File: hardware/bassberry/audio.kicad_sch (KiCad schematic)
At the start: 47 parts, among them J201 SAT LEFT, J202 SAT RIGHT, J203 SUB, U201 TAS5805M, U202 TAS5805M

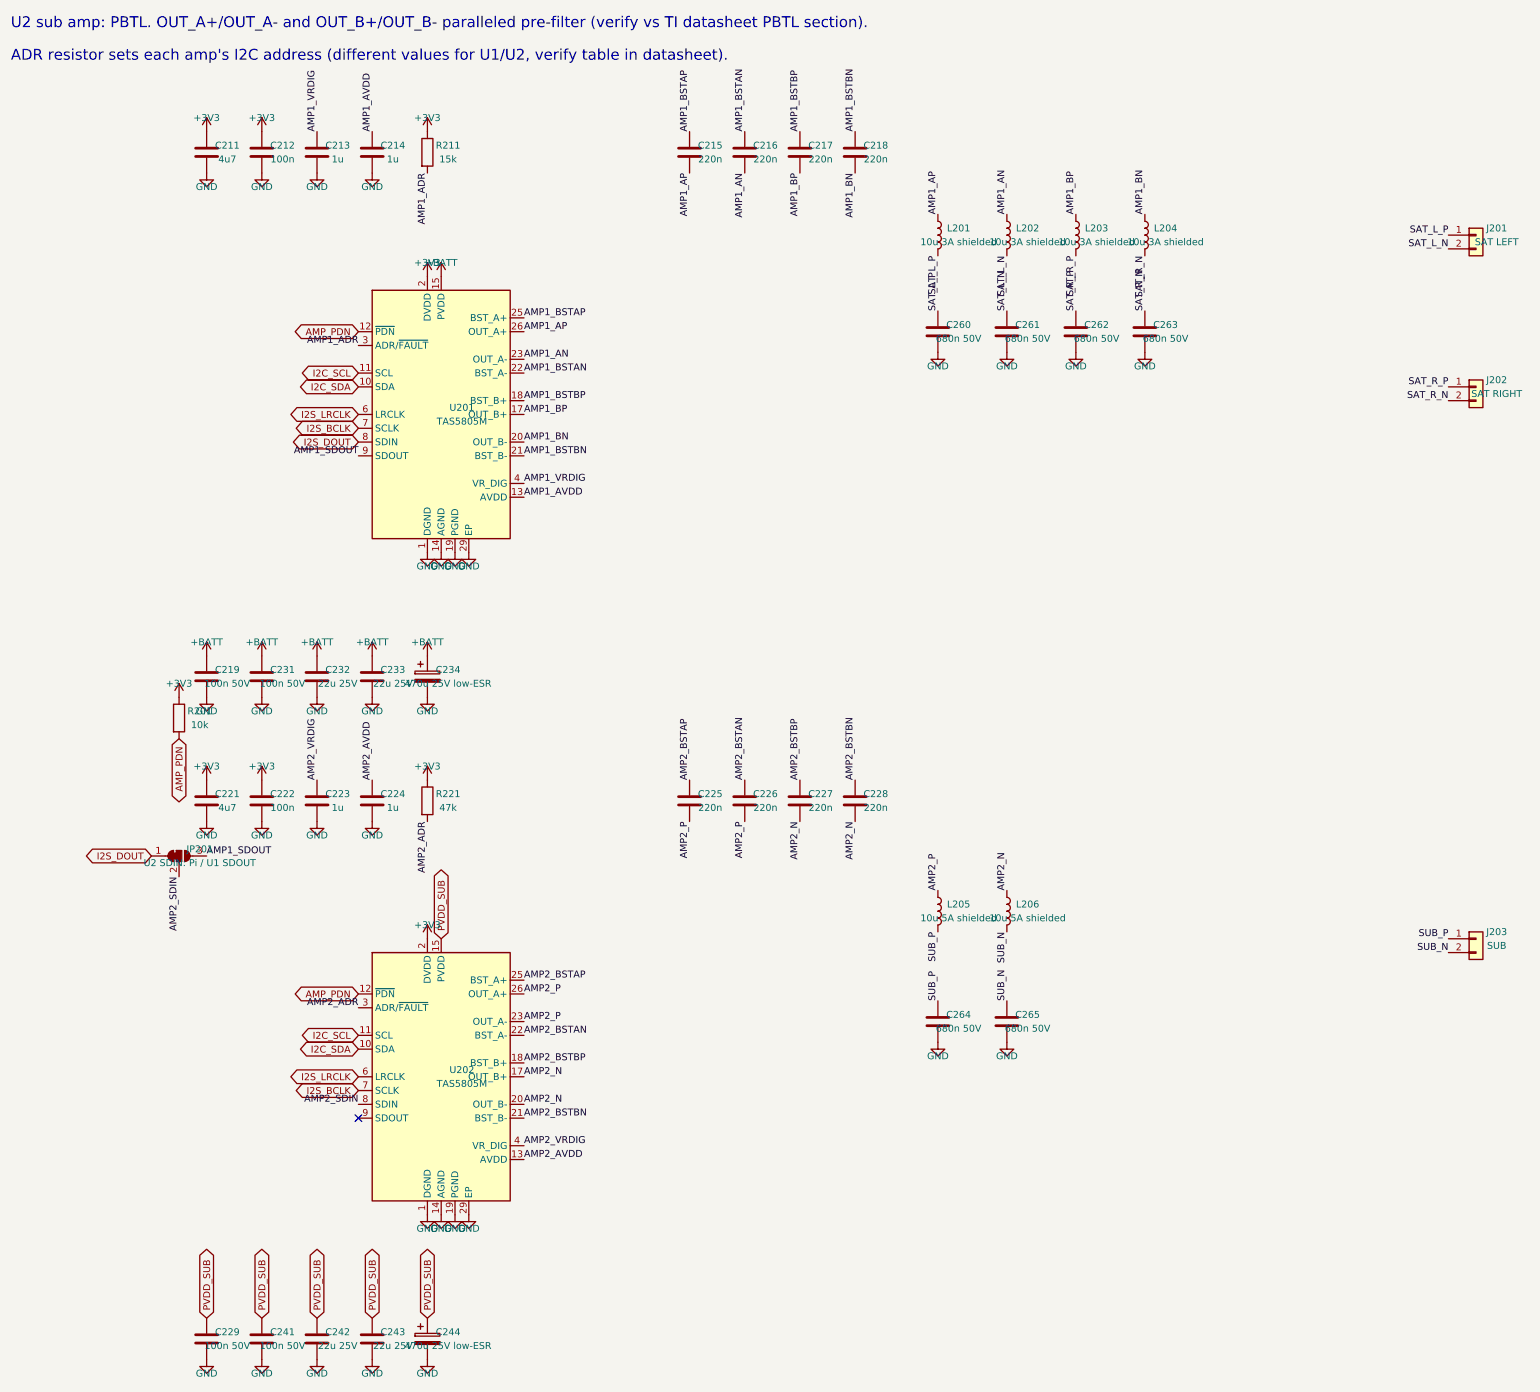
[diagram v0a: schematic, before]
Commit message: rev 0.2 board: routed with srouter, DRC 0 errors / 0 unconnected / 0 parity, digital twin 1-4 PASS; KiCad files, reports, renders
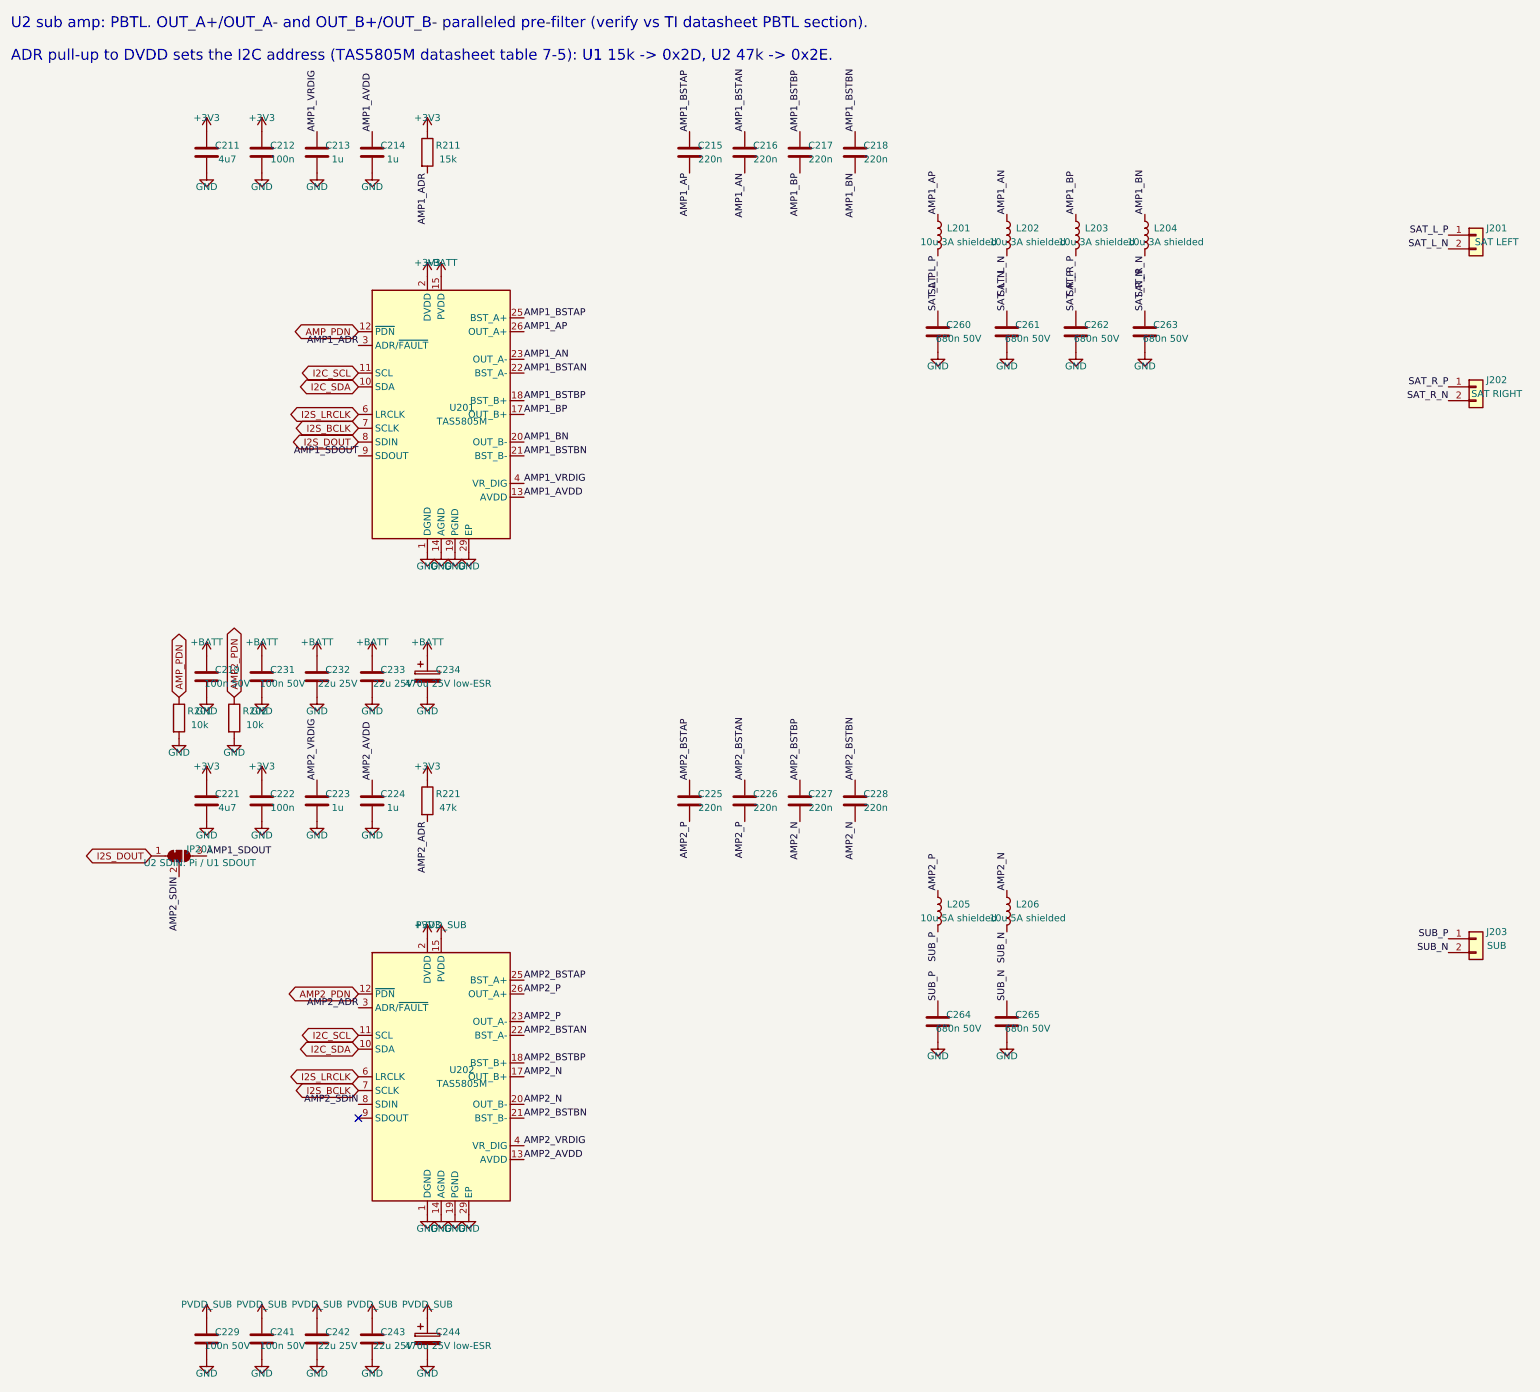
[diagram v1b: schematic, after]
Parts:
- added R202: 10k, Resistor_SMD:R_0603_1608Metric, symbol Device:R
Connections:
- net +3V3: no longer R201.1
- net AMP_PDN: now also R201.1; no longer R201.2, U202.12 (~{PDN})
- net GND: now also R201.2, R202.2
- new net AMP2_PDN: R202.1, U202.12 (~{PDN})
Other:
- note added: "ADR pull-up to DVDD sets the I2C address (TAS5805M datasheet table 7-5): U1 15k -> 0x2D, U2 47k -> 0x2E."
- note removed: "ADR resistor sets each amp's I2C address (different values for U1/U2, verify table in datasheet)."
